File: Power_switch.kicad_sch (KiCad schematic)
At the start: 36 parts, among them Q409 AO3400A, Q410 HSBA8119, Q415 MMBT5551, Q416 AO3400A, Q417 HSBA8119, SW401 SW_SPDT, U400 INA219AIDCNR, U407 INA219AIDCNR, U408 INA219AIDCNR

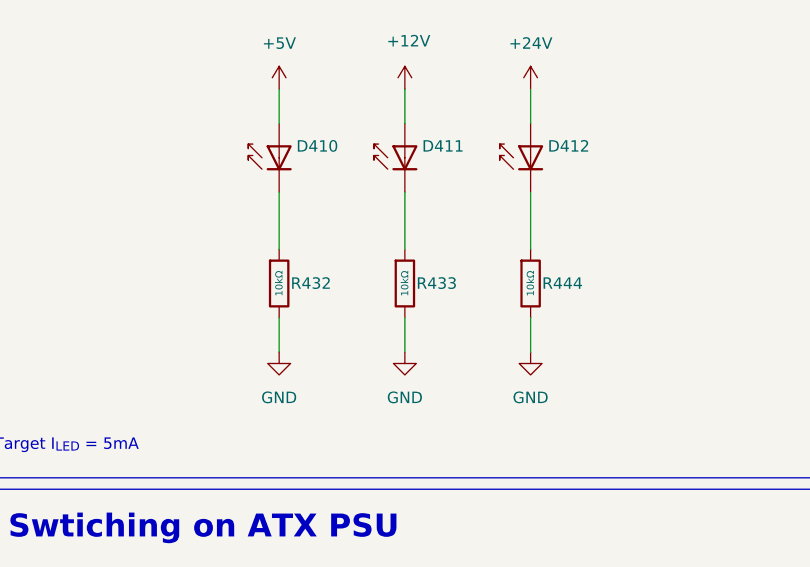
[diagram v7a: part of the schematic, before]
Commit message: updated LED resistor values
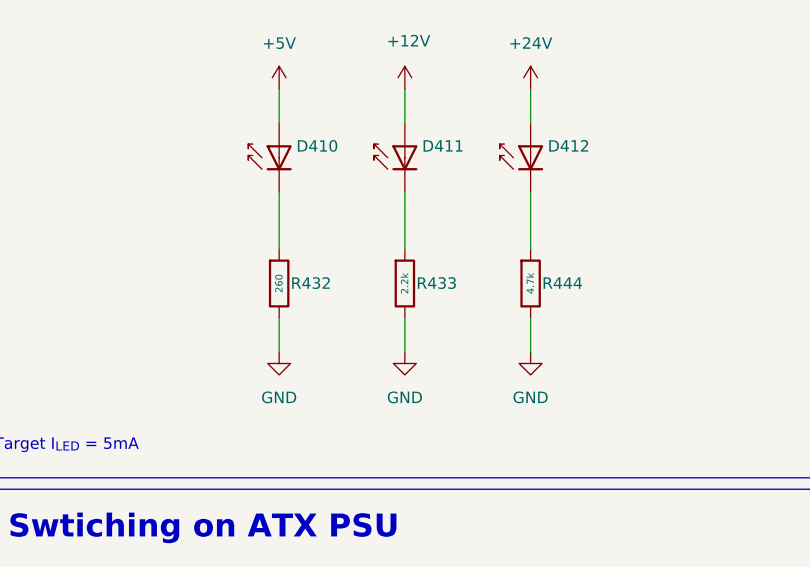
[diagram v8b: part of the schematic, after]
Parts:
- R432: value 10kΩ -> 260
- R433: value 10kΩ -> 2.2k
- R444: value 10kΩ -> 4.7k
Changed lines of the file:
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@@
 			)
 		)
-		(property "Value" "10kΩ"
+		(property "Value" "260"
 			(at 212.09 54.61 90)
 			(do_not_autoplace yes)
@@
 			)
 		)
-		(property "Value" "10kΩ"
+		(property "Value" "2.2k"
 			(at 226.06 54.61 90)
 			(do_not_autoplace yes)
@@
 			)
 		)
-		(property "Value" "10kΩ"
+		(property "Value" "4.7k"
 			(at 240.03 54.61 90)
 			(do_not_autoplace yes)
